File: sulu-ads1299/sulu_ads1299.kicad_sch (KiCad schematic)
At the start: 49 parts, among them J1 Conn_01x08, J2 Conn_02x15_Odd_Even, J3 Conn_01x02, J4 Conn_02x05_Odd_Even, SW1 SW_DIP_x02, U1 TPS62222DDCT, U2 S-85S1AB11-I6T1U, U3 LM2775DSG

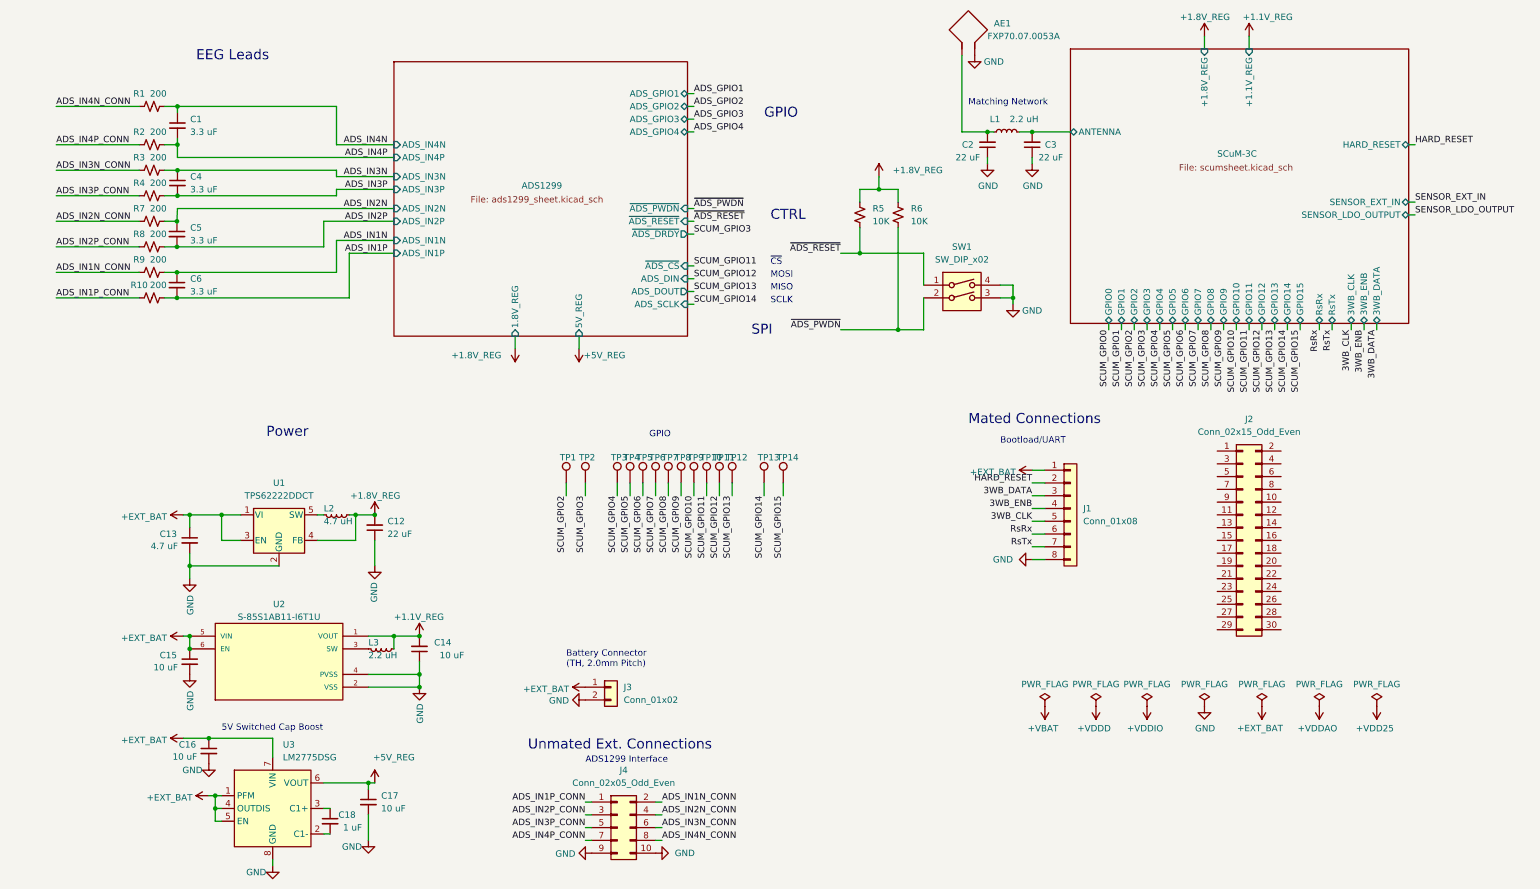
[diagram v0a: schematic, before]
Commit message: Silkscreen cleaned, reduced TP footprint #, post design review
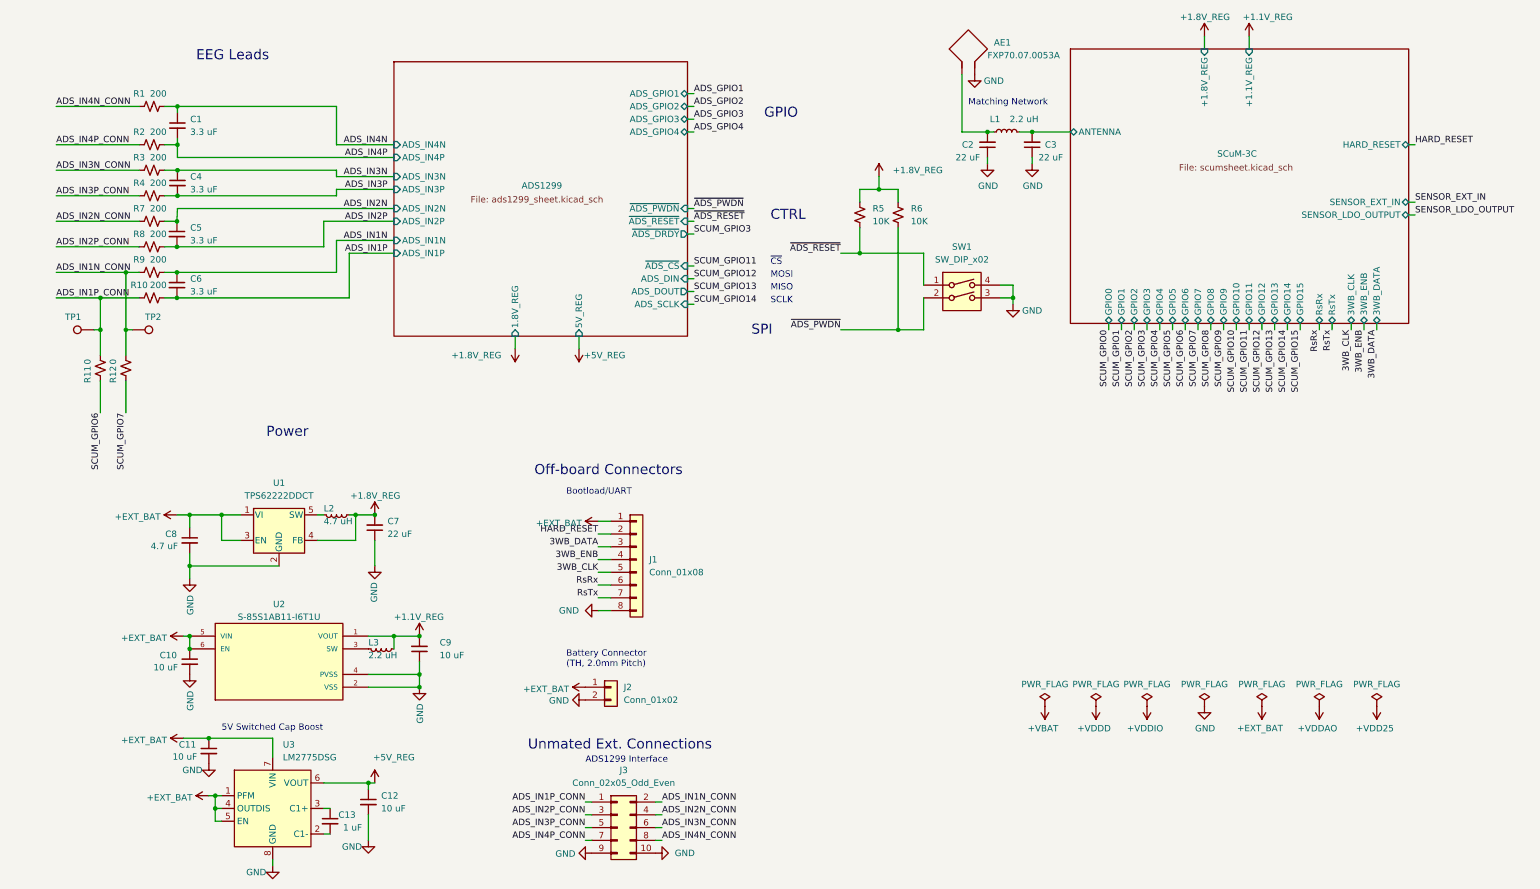
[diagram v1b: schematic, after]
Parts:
- removed J2: Conn_02x15_Odd_Even, symbol Connector_Generic:Conn_02x15_Odd_Even
- removed TP10, TP11, TP12, TP13, TP14, TP3, TP4, TP5, TP6, TP7, TP8, TP9: TestPoint, SCUM:through_hole, symbol Connector:TestPoint
- added R11, R12: 0, Resistor_SMD:R_0402_1005Metric, symbol Device:R_Small_US
- renumbered C15 to C10, C16 to C11, C17 to C12, C18 to C13, C12 to C7, C13 to C8, C14 to C9, J3 to J2, J4 to J3
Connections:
- net ADS_IN1N_CONN: now also TP2.1, R12.2
- net ADS_IN1P_CONN: now also TP1.1, R11.2
- net SCUM_GPIO2: no longer TP1.1
- net SCUM_GPIO3: no longer TP2.1
- net SCUM_GPIO6: now also R11.1
- net SCUM_GPIO7: now also R12.1
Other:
- note added: "Off-board Connectors"
- note removed: "Mated Connections"
- moved on the sheet: AE1, J1

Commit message: Sulu-ADS1299 rev2 commit before changing 1.1V regulator
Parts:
- added U?: TLV71311PDBV, Package_TO_SOT_SMD:SOT-23-5, symbol Regulator_Linear:TLV71311PDBV
- added U?: TLV70018_SOT353, Package_TO_SOT_SMD:SOT-353_SC-70-5, symbol Regulator_Linear:TLV70018_SOT353
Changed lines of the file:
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@@
     (pin "1")
+  )
+  (symbol (lib_id "Regulator_Linear:TLV71311PDBV") (at 11.43 147.32 0) (unit 1)
+    (in_bom yes) (on_board yes) (fields_autoplaced)
+    (property "Reference" "U?" (id 0) (at 11.43 137.16 0))
+    (property "Value" "TLV71311PDBV" (id 1) (at 11.43 139.7 0))
+    (property "Footprint" "Package_TO_SOT_SMD:SOT-23-5" (id 2) (at 11.43 139.065 0)
+      (effects (font (size 1.27 1.27) italic) hide)
+    )
+    (property "Datasheet" "http://www.ti.com/lit/ds/symlink/tlv713p.pdf" (id 3) (at 11.43 146.05 0)
+      (effects (font (size 1.27 1.27)) hide)
+    )
+    (pin "1")
+    (pin "2")
+    (pin "3")
+    (pin "4")
+    (pin "5")
   )
   (symbol (lib_id "Connector_Generic:Conn_01x02") (at 123.19 147.32 0) (unit 1)
@@
     (pin "1")
   )
+  (symbol (lib_id "Regulator_Linear:TLV70018_SOT353") (at 90.17 99.06 0) (unit 1)
+    (in_bom yes) (on_board yes) (fields_autoplaced)
+    (property "Reference" "U?" (id 0) (at 90.17 88.9 0))
+    (property "Value" "TLV70018_SOT353" (id 1) (at 90.17 91.44 0))
+    (property "Footprint" "Package_TO_SOT_SMD:SOT-353_SC-70-5" (id 2) (at 90.17 91.44 0)
+      (effects (font (size 1.27 1.27) italic) hide)
+    )
+    (property "Datasheet" "http://www.ti.com/lit/ds/symlink/tlv700.pdf" (id 3) (at 90.17 97.79 0)
+      (effects (font (size 1.27 1.27)) hide)
+    )
+    (pin "1")
+    (pin "2")
+    (pin "3")
+    (pin "4")
+    (pin "5")
+  )
   (symbol (lib_id "Device:R_Small_US") (at 172.72 53.34 0) (unit 1)
     (in_bom yes) (on_board yes) (fields_autoplaced)
@@
       (reference "J8") (unit 1) (value "through_hole") (footprint "SCUM:through_hole")
     )
-    (path "/1f92f92f-1391-4fc3-892c-7c652348c5b5/bcf7a9bb-1e12-41af-b6bf-453de278257d"
-      (reference "J9") (unit 1) (value "through_hole") (footprint "SCUM:through_hole")
-    )
     (path "/1f92f92f-1391-4fc3-892c-7c652348c5b5/5adceea1-6536-46e4-9ff0-fcc4ec0d2cc8"
       (reference "J11") (unit 1) (value "through_hole") (footprint "SCUM:through_hole")
@@
       (reference "J17") (unit 1) (value "through_hole") (footprint "SCUM:through_hole")
     )
-    (path "/1f92f92f-1391-4fc3-892c-7c652348c5b5/addfd10d-e38f-411b-8533-2d70d6d1aa61"
-      (reference "J18") (unit 1) (value "through_hole") (footprint "SCUM:through_hole")
-    )
-    (path "/1f92f92f-1391-4fc3-892c-7c652348c5b5/535304ec-2aba-4247-819e-ec22f480a68f"
-      (reference "J19") (unit 1) (value "through_hole") (footprint "SCUM:through_hole")
-    )
     (path "/1f92f92f-1391-4fc3-892c-7c652348c5b5/b3a4ce07-043e-414d-9f6a-f264178ab753"
       (reference "J20") (unit 1) (value "through_hole") (footprint "SCUM:through_hole")
@@
       (reference "U5") (unit 1) (value "scum3") (footprint "SCUM:QFN-100_EP_12x12_Pitch0.4mm_Margin0.25mm")
     )
-  )
+    (path "/3ec5049a-873c-4e70-8616-805c46538e39"
+      (reference "U?") (unit 1) (value "TLV71311PDBV") (footprint "Package_TO_SOT_SMD:SOT-23-5")
+    )
+    (path "/dd53f162-3abd-4e3a-b0fc-66af82dd1158"
+      (reference "U?") (unit 1) (value "TLV70018_SOT353") (footprint "Package_TO_SOT_SMD:SOT-353_SC-70-5")
+    )
+  )

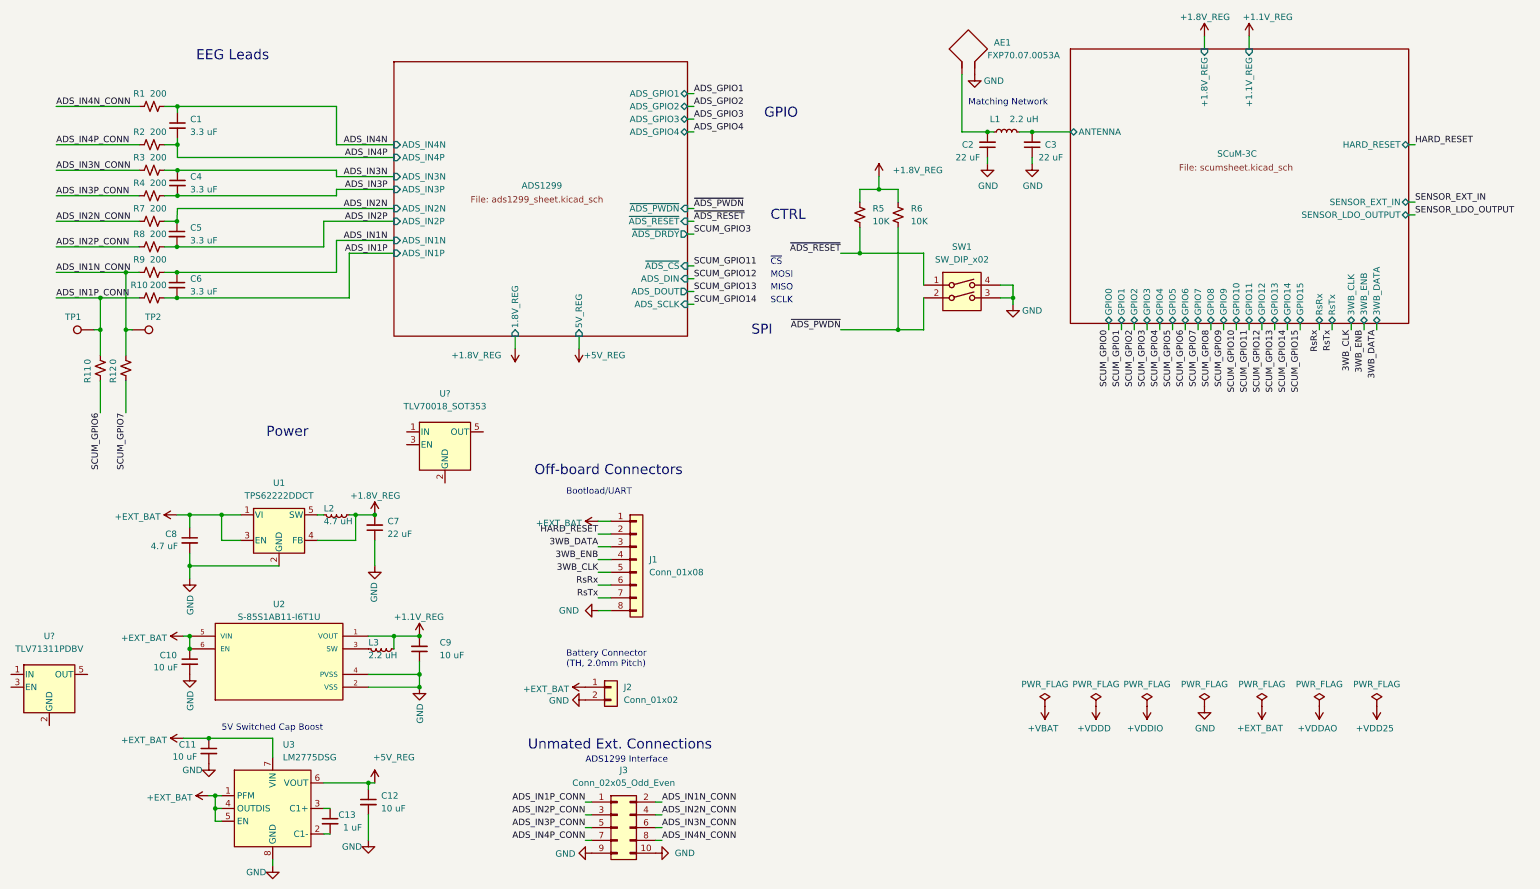
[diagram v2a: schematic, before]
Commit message: BOM adjustments, protection Zener diodes, JLCPCB fab files
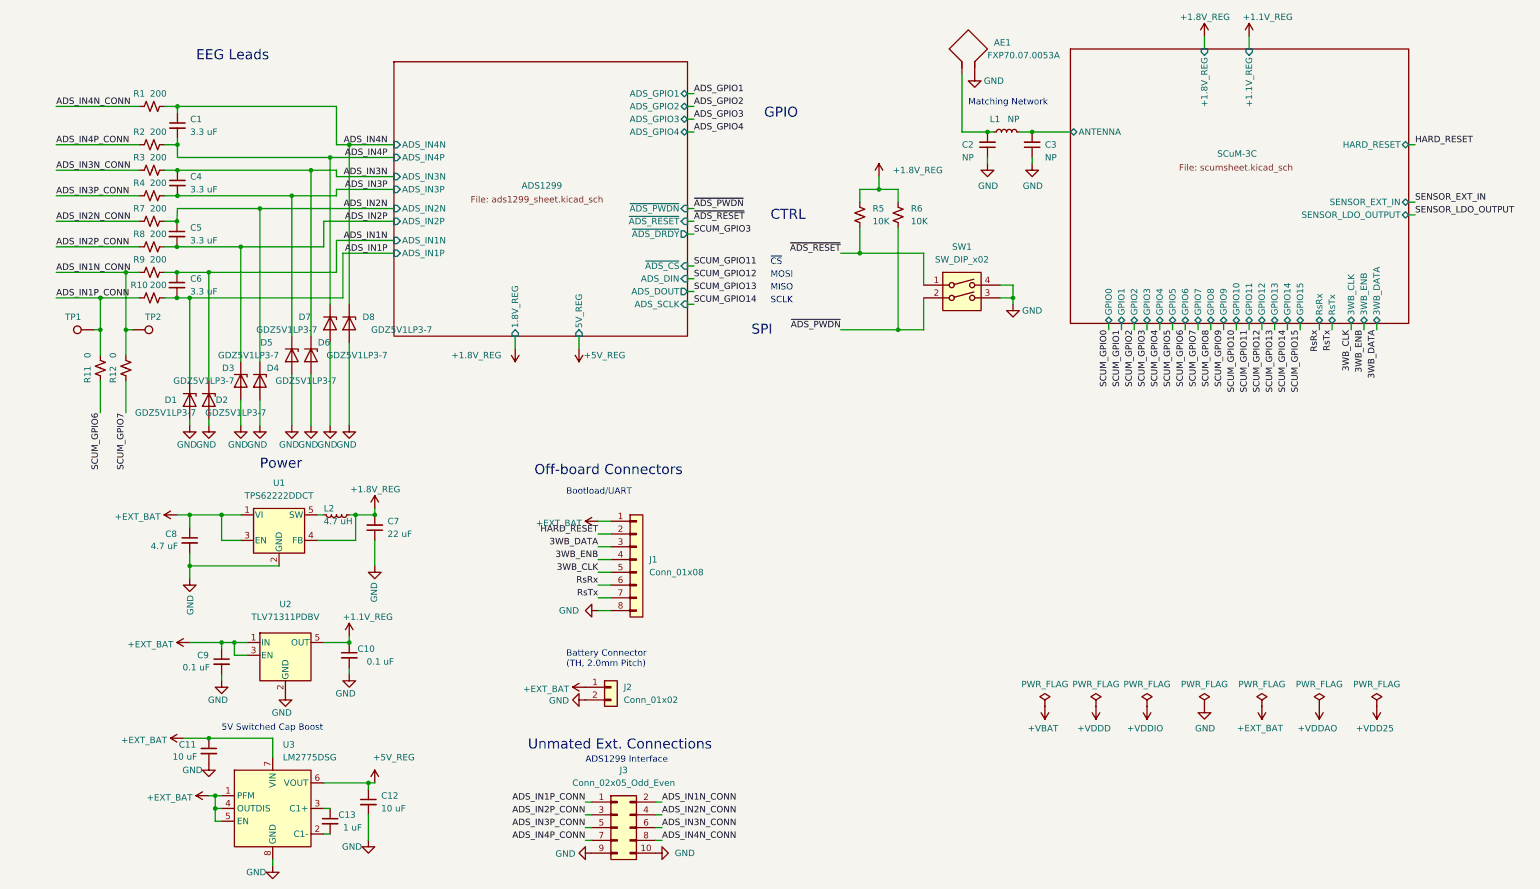
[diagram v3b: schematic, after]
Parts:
- removed L3: 2.2 uH, Inductor_SMD:L_Wuerth_MAPI-2010, symbol Device:L_Small
- removed U2: S-85S1AB11-I6T1U, downloaded_libs:SOFL50P180X50-6N, symbol S-85S1AB20-I6T1U:S-85S1AB11-I6T1U
- removed U?: TLV70018_SOT353, Package_TO_SOT_SMD:SOT-353_SC-70-5, symbol Regulator_Linear:TLV70018_SOT353
- added D1, D2, D3, D4, D5, D6, D7, D8: GDZ5V1LP3-7, Diode_SMD:D_0201_0603Metric, symbol Diode:BZV55B5V1
- C10, C9: value 10 uF -> 0.1 uF
- C2, C3: value 22 uF -> NP
- C7: footprint Capacitor_SMD:C_0402_1005Metric -> Capacitor_SMD:C_0603_1608Metric
- J3: footprint Connector_PinSocket_2.54mm:PinSocket_2x05_P2.54mm_Vertical_SMD -> Connector_PinHeader_2.54mm:PinHeader_2x05_P2.54mm_Vertical_SMD
- L1: value 2.2 uH -> NP
- gave numbers to parts that had none: 1
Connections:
- net +1.1V_REG: now also C10.1, U2.5 (OUT); no longer C9.2
- net +EXT_BAT: now also C9.1, U2.1 (IN), U2.3 (EN); no longer C10.1
- net ADS_IN1N: now also D2.1 (K)
- net ADS_IN1P: now also D1.1 (K)
- net ADS_IN2N: now also D4.1 (K)
- net ADS_IN2P: now also D3.1 (K)
- net ADS_IN3N: now also D6.1 (K)
- net ADS_IN3P: now also D5.1 (K)
- net ADS_IN4N: now also D8.1 (K)
- net ADS_IN4P: now also D7.1 (K)
- net GND: now also C9.2, U2.2 (GND), D1.2 (A), D2.2 (A), D3.2 (A), D4.2 (A), D5.2 (A), D6.2 (A), D7.2 (A), D8.2 (A); no longer C9.1
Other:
- moved on the sheet: U2

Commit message: Final submitted layout, gerbers, drill files, bom, and cpl
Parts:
- J3: footprint Connector_PinHeader_2.54mm:PinHeader_2x05_P2.54mm_Vertical_SMD -> Connector_PinSocket_2.54mm:PinSocket_2x05_P2.54mm_Vertical_SMD
- SW1: footprint Button_Switch_SMD:SW_DIP_SPSTx02_Slide_6.7x6.64mm_W6.73mm_P2.54mm_LowProfile_JPin -> eec:CK_Components-TDA02H0SB1-MFG
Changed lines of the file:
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@@
     (property "Reference" "SW1" (id 0) (at 193.04 59.69 0))
     (property "Value" "SW_DIP_x02" (id 1) (at 193.04 62.23 0))
-    (property "Footprint" "Button_Switch_SMD:SW_DIP_SPSTx02_Slide_6.7x6.64mm_W6.73mm_P2.54mm_LowProfile_JPin" (id 2) (at 193.04 69.85 0)
+    (property "Footprint" "eec:CK_Components-TDA02H0SB1-MFG" (id 2) (at 193.04 69.85 0)
       (effects (font (size 1.27 1.27)) hide)
     )
@@
     (property "Reference" "J3" (id 0) (at 125.73 163.83 0))
     (property "Value" "Conn_02x05_Odd_Even" (id 1) (at 125.73 166.37 0))
-    (property "Footprint" "Connector_PinHeader_2.54mm:PinHeader_2x05_P2.54mm_Vertical_SMD" (id 2) (at 124.46 175.26 0)
+    (property "Footprint" "Connector_PinSocket_2.54mm:PinSocket_2x05_P2.54mm_Vertical_SMD" (id 2) (at 124.46 175.26 0)
       (effects (font (size 1.27 1.27)) hide)
     )
@@
     )
     (path "/c3908c37-c7aa-4ce8-9ced-e52d8179e2ca"
-      (reference "J3") (unit 1) (value "Conn_02x05_Odd_Even") (footprint "Connector_PinHeader_2.54mm:PinHeader_2x05_P2.54mm_Vertical_SMD")
+      (reference "J3") (unit 1) (value "Conn_02x05_Odd_Even") (footprint "Connector_PinSocket_2.54mm:PinSocket_2x05_P2.54mm_Vertical_SMD")
     )
     (path "/1f92f92f-1391-4fc3-892c-7c652348c5b5/103e8f34-79cf-4f47-9291-d2d2203a295a"
@@
     )
     (path "/1bb106ea-ac1b-46fa-8465-e7cc217a10a6"
-      (reference "SW1") (unit 1) (value "SW_DIP_x02") (footprint "Button_Switch_SMD:SW_DIP_SPSTx02_Slide_6.7x6.64mm_W6.73mm_P2.54mm_LowProfile_JPin")
+      (reference "SW1") (unit 1) (value "SW_DIP_x02") (footprint "eec:CK_Components-TDA02H0SB1-MFG")
     )
     (path "/69394886-050d-4abd-af2a-a30cd096402c"
